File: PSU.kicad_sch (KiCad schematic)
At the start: 97 parts, among them Q1001 2N7002, Q1002 2N7002, Q1003 2N7002, Q1004 2N7002, Q1005 2N7002, Q1006 2N7002, Q1007 AO3407, Q5 2N7002, Q6 2N7002, Q7 NCE30P28Q, SW1001 SW_Push, SW1002 SW_Push, U1001 HM7533HBPR, U1002 SY8253ADC, U1003 SY8253ADC, U1005 TL431DBZ

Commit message: commit before removing duplicated glasgow
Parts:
- renumbered C1039 to C160, C1040 to C161, C1001 to C162, C1002 to C163, C1003 to C164, C1004 to C165, C1005 to C166, C1006 to C167, C1007 to C168, C1008 to C169, C1009 to C170, C1010 to C171, C1011 to C172, C1012 to C173, C1013 to C174, C1014 to C175, C1015 to C176, C1016 to C177, C1017 to C178, C1018 to C179, C1019 to C180, C1020 to C181, C1021 to C182, C1022 to C183, C1023 to C184, D1001 to D27, D1002 to D28, D1003 to D29, D1004 to D30, D23 to D31, D1005 to D32, D1006 to D33, D1007 to D34, D1008 to D35, D1009 to D36, F1001 to F5, JP1001 to JP1, JP1002 to JP2, JP1003 to JP3, L1001 to L3, L1002 to L4, NT1001 to NT2, Q5 to Q1, Q1007 to Q10, Q6 to Q2, Q7 to Q3, Q1001 to Q4, Q1002 to Q5, Q1003 to Q6, Q1004 to Q7, Q1005 to Q8, Q1006 to Q9, R1007 to R100, R1008 to R101, R1009 to R102, R1010 to R103, R1011 to R104, R1012 to R105, R1013 to R106, R1014 to R107, R1015 to R108, R1016 to R109, R1017 to R110, R1018 to R111, R1019 to R112, R1020 to R113, R1021 to R114, R1022 to R115, R1023 to R116, R1024 to R117, R1025 to R118, R1030 to R86, R1031 to R87, R1032 to R88, R1033 to R89, R1034 to R90, R1035 to R91, R1001 to R92, R1002 to R93, R1036 to R94, R1003 to R95, R1004 to R96, R1005 to R97, R54 to R98, R1006 to R99, SW1001 to SW2, SW1002 to SW3, TP1001 to TP22, TP8 to TP23, TP1002 to TP24, TP1003 to TP25, TP1004 to TP26, TP1005 to TP27, U1005 to U39, U1001 to U40, U1002 to U41, U1003 to U42

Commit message: is this a differential pair?
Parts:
- C167: SCH_Show_Footprint (none) -> C0402
- D27: SCH_Show_Footprint (none) -> SMA
- D33: SCH_Show_Footprint (none) -> SOD-323
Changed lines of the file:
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@@
 			)
 		)
+		(property "Field-1" ""
+			(at 255.27 281.94 0)
+			(effects
+				(font
+					(size 1.27 1.27)
+				)
+				(hide yes)
+			)
+		)
+		(property "SCH_Show_Footprint" ""
+			(at 255.27 281.94 0)
+			(effects
+				(font
+					(size 1.27 1.27)
+				)
+				(hide yes)
+			)
+		)
 		(pin "1"
 		)
@@
 			)
 		)
+		(property "Field-1" ""
+			(at 299.72 280.67 0)
+			(effects
+				(font
+					(size 1.27 1.27)
+				)
+				(hide yes)
+			)
+		)
 		(pin "3"
 		)
@@
 			)
 		)
+		(property "Field-1" ""
+			(at 276.86 281.94 0)
+			(effects
+				(font
+					(size 1.27 1.27)
+				)
+				(hide yes)
+			)
+		)
+		(property "SCH_Show_Footprint" ""
+			(at 276.86 281.94 0)
+			(effects
+				(font
+					(size 1.27 1.27)
+				)
+				(hide yes)
+			)
+		)
 		(pin "1"
 		)
@@
 			)
 		)
+		(property "Field-1" ""
+			(at 111.76 127 0)
+			(effects
+				(font
+					(size 1.27 1.27)
+				)
+				(hide yes)
+			)
+		)
+		(property "SCH_Show_Footprint" "SMA"
+			(at 111.76 127 0)
+			(effects
+				(font
+					(size 1.27 1.27)
+				)
+				(hide yes)
+			)
+		)
 		(pin "1"
 		)
@@
 			)
 		)
+		(property "Field-1" ""
+			(at 269.24 281.94 0)
+			(effects
+				(font
+					(size 1.27 1.27)
+				)
+				(hide yes)
+			)
+		)
+		(property "SCH_Show_Footprint" "SOD-323"
+			(at 269.24 281.94 0)
+			(effects
+				(font
+					(size 1.27 1.27)
+				)
+				(hide yes)
+			)
+		)
 		(pin "1"
 		)
@@
 			(at 255.27 294.64 0)
 			(effects
+				(font
+					(size 1.27 1.27)
+				)
+				(hide yes)
+			)
+		)
+		(property "Field-1" ""
+			(at 255.27 294.64 0)
+			(effects
+				(font
+					(size 1.27 1.27)
+				)
+				(hide yes)
+			)
+		)
+		(property "SCH_Show_Footprint" "C0402"
+			(at 255.27 294.64 0)
+			(effects

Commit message: went back to the drawing board
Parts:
- removed C160, C161, C171, C184: 1uF/16V, A_HDJ_Library:C_0402_1005Metric, symbol Device:C
- removed C162, C163, C164, C165: 22uF/25V, Capacitor_SMD:C_0805_2012Metric, symbol Device:C
- removed C166, C168: 2.2uF/50V, A_DFRobot:C_0603, symbol YXD:C
- removed C167: 10uF/10V, A_HDJ_Library:C_0402_1005Metric, symbol Device:C
- removed C169, C170, C179: 100nF/16V, A_HDJ_Library:C_0402_1005Metric, symbol Device:C
- removed C173: 12pF/50V, Capacitor_SMD:C_0402_1005Metric, symbol Device:C
- removed C175, C177, C180, C181, C182, C183: 22uF/10V, A_HDJ_Library:C_0603_1608Metric, symbol Device:C
- removed D27: SMAJ26CA, A_DFRobot:D_SMA, symbol Diode_TVS_AKL:SMAJ24CA
- removed D28, D29, D30: SS54, A_DFRobot:D_SMA, symbol Device:D_Schottky
- removed D31, D34: LED_G, A_HDJ_Library:LED_0603_1608Metric, symbol Device:LED
- removed D33: 1N5819WS, A_DFRobot:D_SOD-323, symbol Diode:1N5819WS
- removed F5: BSMD1206C-2100T, A_DFRobot:R_1206, symbol Device:Fuse
- removed JP1: Jumper_3_Bridged12, A_HDJ_Library:PinHeader_1x03_P2.54mm_Vertical, symbol Jumper:Jumper_3_Bridged12
- removed JP2: Jumper_3_Bridged12, A_DFRobot:PinHeader_1x03_P2.54mm_Vertical, symbol Jumper:Jumper_3_Bridged12
- removed JP3: ~, Connector_PinHeader_2.54mm:PinHeader_2x03_P2.54mm_Vertical, symbol YXD:Pin_2*3
- removed L3, L4: 2.2uH/4.3A, A_HDJ_Library:L_Sunlord_SWPA4020S, symbol Device:L
- removed NT2: NetTie_2, NetTie:NetTie-3_SMD_Pad2.0mm, symbol Device:NetTie_2
- removed Q1, Q2, Q5, Q6, Q7, Q8, Q9: 2N7002, Package_TO_SOT_SMD:SOT-23, symbol Transistor_FET:2N7002
- removed Q10: AO3407, Package_TO_SOT_SMD:SOT-23, symbol Transistor_FET:Q_PMOS_GSD
- removed Q3: NCE30P28Q, A_HDJ_Library:MOSFET_PDFN8_3.3x3.3, symbol Transistor_FET:AON7262E
- removed R101: 1M/1%, A_DFRobot:R_0402, symbol Device:R
- removed R102, R91, R94, R99: 100K/1%, A_DFRobot:R_0402, symbol Device:R
- removed R103, R104, R95: 1K/1%, A_DFRobot:R_0402, symbol Device:R
- removed R105, R110, R118, R86, R88, R97: 10K/1%, A_DFRobot:R_0402, symbol Device:R
- removed R106: 470R/1%, A_DFRobot:R_0402, symbol Device:R
- removed R107, R87: 2.2K/1%, A_DFRobot:R_0402, symbol Device:R
- removed R108, R113, R92, R93, R96: 100R/1%, A_DFRobot:R_0402, symbol Device:R
- removed R111, R89, R90, R98: 21.5K/1%, A_DFRobot:R_0402, symbol Device:R
- removed R112: 4.7K/1%, A_DFRobot:R_0402, symbol Device:R
- removed R115: 200R/1%, A_DFRobot:R_0402, symbol YXD:R
- removed TP22, TP23, TP24, TP25, TP26, TP27: TestPoint, A_HDJ_Library:TestPoint_Pad_D1.5mm, symbol Connector:TestPoint
- removed U39: TL431DBZ, A_HDJ_Library:SOT-23, symbol Reference_Voltage:TL431DBZ
- removed U40: HM7533HBPR, Package_TO_SOT_SMD:SOT-89-3, symbol YXD:HM7533
- removed U41, U42: SY8253ADC, A_HDJ_Library:TSOT-23-6, symbol Regulator_Switching:LM2734X
- added C1: 0.1uF, A_HDJ_Library:C_0402_1005Metric, symbol Device:C
- added C2: 10uF, Capacitor_SMD:C_0805_2012Metric, symbol Device:C
- added C3, C4, C5, C6: 10uF 25V, Capacitor_SMD:C_0805_2012Metric, symbol Device:C
- added C401: 100nF/50V, A_HDJ_Library:C_0402_1005Metric, symbol Device:C
- added C408: 22uF/50V, Capacitor_SMD:C_0805_2012Metric, symbol Device:C
- added C410, C411, C412, C413: 1uF/50V, A_HDJ_Library:C_0402_1005Metric, symbol Device:C
- added C414, C415: 0.1uf, A_HDJ_Library:C_0402_1005Metric, symbol Device:C
- added C416, C417: 100uF, A_HDJ_Library:C_0402_1005Metric, symbol Device:C
- added L401: 6.8uH/4.5A, Inductor_SMD:L_6.3x6.3_H3, symbol Device:L
- added R402: 19.1K/1%, A_HDJ_Library:R_0402_1005Metric, symbol Device:R
- added R405, R408: 1K/1%, A_HDJ_Library:R_0402_1005Metric, symbol Device:R
- added R409: 10K/1%, A_HDJ_Library:R_0402_1005Metric, symbol Device:R
- added U3: TPPM0110DWPR, DWP20_3P81X2P79, symbol 2026-04-06_00-39-49:TPPM0110DWPR
- added U402: AP7381-33SA-7, Package_TO_SOT_SMD:SOT-23, symbol Regulator_Linear:AP7381-33SA-7
- added U403: AP63200WU, Package_TO_SOT_SMD:TSOT-23-6, symbol Regulator_Switching:AP63200WU
- C402: renamed from C172; value 12pF/50V -> 47pF/50V; footprint Capacitor_SMD:C_0402_1005Metric -> A_HDJ_Library:C_0402_1005Metric; DF_Comment 贴片电容0402-12pF-50V-NPO(0402) -> (none); Digikey (none) -> 490-5942-1-ND; now fitted; now in the parts list
- C403: renamed from C174; DF_Comment 贴片电容0603-22uF-10V-X5R(0603) -> (none); Digikey (none) -> 490-10476-1-ND
- C404: renamed from C176; DF_Comment 贴片电容0603-22uF-10V-X5R(0603) -> (none); Digikey (none) -> 490-10476-1-ND
- C405: renamed from C178; value 100nF/16V -> 100nF/50V; DF_Comment 贴片电容0402-100nF-16V-X7R(0402) -> (none); Digikey (none) -> 478-KGM05CR71H104KHCT-ND
- D401: renamed from D35; value 0402ESDA-05N -> ESD5V0B03; DF_Comment 5.0V双向静电保护管_0402ESDA-05N -> (none); Digikey (none) -> ESD9B5.0ST5GOSCT-ND
- D402: renamed from D36; value 0402ESDA-05N -> ESD5V0B03; DF_Comment 5.0V双向静电保护管_0402ESDA-05N -> (none); Digikey (none) -> ESD9B5.0ST5GOSCT-ND
- D403: renamed from D32; value LED_R -> LED_G; DF_Comment 贴片LED红色0603(0603) -> (none); Digikey (none) -> 160-1479-1-ND
- Q401: renamed from Q4; footprint Package_TO_SOT_SMD:SOT-23 -> A_HDJ_Library:SOT-23; DF_Comment 2N7002-N沟道MOS管-SOT-23[备选型号:JMTL2N7002K] -> (none); Digikey (none) -> 2N7002-TPMSCT-ND
- R401: renamed from R109; value 75K/1% -> 100K/1%; footprint A_DFRobot:R_0402 -> A_HDJ_Library:R_0402_1005Metric; DF_Comment 贴片电阻0402-75K-1% -> (none); Digikey (none) -> 311-100KJRCT-ND
- R403: renamed from R114; DF_Comment 贴片电阻0402-10K-1% -> (none)
- R404: renamed from R117; DF_Comment 贴片电阻0402-10K-1% -> (none)
- R406: renamed from R116; value 100R/1% -> 1K/1%; footprint A_DFRobot:R_0402 -> A_HDJ_Library:R_0402_1005Metric; DF_Comment 贴片电阻0402-100R-1% -> (none); Digikey (none) -> 311-1.0KJRCT-ND
- R407: renamed from R100; value 2.2K/1% -> 1K/1%; footprint A_DFRobot:R_0402 -> A_HDJ_Library:R_0402_1005Metric; DF_Comment 贴片电阻0402-2.2K-1% -> (none); Digikey (none) -> 311-1.0KJRCT-ND
- SW401: renamed from SW2; footprint A_DFRobot:SW_PUSH_SIDE_TS-1012EV_7.7x3.95x3.5mm -> Button_Switch_THT:SW_PUSH_6mm; DF_Comment 侧按卧插4脚开关-TS-1012EV-26-7*3.5*3.5 -> (none); Digikey (none) -> 450-1644-ND
- SW402: renamed from SW3; footprint A_DFRobot:SW_PUSH_SIDE_TS-1012EV_7.7x3.95x3.5mm -> Button_Switch_THT:SW_PUSH_6mm; DF_Comment 侧按卧插4脚开关-TS-1012EV-26-7*3.5*3.5 -> (none); Digikey (none) -> 450-1644-ND
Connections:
- net +3V3_ROM is gone; now on net +3V3: R407.2
- net QGND is gone; now on net GND: C403.1, C404.1, C405.2, D401.1 (A1), D402.1 (A1), Q401.2 (S), SW401.2, SW402.2
- net +12V: now also C1.1, C2.2, C3.2, C4.2, C408.2, C412.1, C5.2, C6.2, U402.1 (VI), U403.2 (EN), U403.3 (IN)
- net +3V3: now also C413.1, C415.2, C417.1, U3.4 (3.3VOUT), U402.2 (VO)
- net +5V: now also L401.2, U3.6 (5VCC)
- net GND: now also C1.2, C2.1, C3.1, C4.1, C408.1, C410.2, C411.2, C412.2, C413.2, C414.1, C415.1, C416.2, C417.2, C5.1, C6.1, R402.1, R409.1, U3.20 (GND), U402.3 (GND), U403.4 (GND)
- net ~{PWR_LED}/~{PSON}: now also R408.1
- net ~{PWR_SW}: now also R405.2
- net at C402.2, R401.1: now also R402.2, U403.1 (FB)
- net at Q401.1 (G): now also R408.2, R409.2
- net POWER_SW: no longer names the net of D401.2 (A2), R403.1, SW401.1
- net POWER_SW: now also C410.1, R405.1
- net RESET_SW: no longer names the net of D402.2 (A2), R404.1, R406.1, SW402.1
- net RESET_SW: now also C411.1
- new net: C401.1, L401.1, U403.5 (SW)
- new net: C401.2, U403.6 (BST)
- new net +1V8: C414.2, C416.1, U3.8 (1.8VOUT)
- no-connect marks 1 -> 0
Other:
- note added: "AP63300 32V 3A 500kHz"
- note added: "LattePanda Mu has integrated pull-up resistors."
- note added: "alternatives? Diodes AP63300 (different vFB)"
- note removed: "12V DC Input(12V 6A-10A)"
- note removed: "Auto PowerUp"
- note removed: "LattePanda Mu has integrated pull-up resistors. Do not solder resistors R50 and R56!"
- note removed: "Power for PCIe x4 OVP@13.86V"
- note removed: "Pullup power for bios_sel"
- note removed: "SY8253ADC 23V 3A 500kHz"
- note removed: "Vout=0.6*(21.5+4.7)/4.7=3.446V"
- note removed: "Vout=0.6*(75+10)/10=5.1V"
- note removed: "soft start"
- moved on the sheet: C403, C404, C405, D401, D402, D403, Q401, R401, R403, R404, R406, R407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

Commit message: some power stuff (unfinished)
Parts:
- added C10, C12, C8, C9: 22uF, 25V, Capacitor_SMD:C_1206_3216Metric, symbol Device:C
- added C40, C41, C42: 1uF, A_DFRobot:C_0402_1005Metric, symbol Device:C
- added C43: 10v 0.1uF, A_DFRobot:C_0402_1005Metric, symbol Device:C
- added C44, C45, C46, C47, C48, C51, C52, C53: 10V 47uF, Capacitor_SMD:C_1210_3225Metric, symbol Device:C
- added C7: 330uF 25V, Capacitor_SMD:CP_Elec_8x11.9, symbol Device:C
- added L1: 550nH, Inductor_SMD:L_Coilcraft_XAL7070-XXX, symbol Device:L
- added NT1: NetTie_2, symbol Device:NetTie_2
- added R16: 200k, A_DFRobot:R_0402_1005Metric, symbol Device:R
- added R18: 100k, A_DFRobot:R_0402_1005Metric, symbol Device:R
- added R19, R20: 0, A_DFRobot:R_0402_1005Metric, symbol Device:R
- added U4: TPS548A23VANR, VAN0019A-MFG, symbol 2026-04-07_02-11-45:TPS548A23VANR
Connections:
- net +12V: now also C10.1, C12.1, C40.1, C41.1, C7.1, C8.1, C9.1, R16.1, U4.12 (VIN), U4.4 (VIN)
- net GND: now also C10.2, C12.2, C40.2, C41.2, C42.1, C44.1, C45.1, C46.1, C47.1, C48.1, C51.1, C52.1, C53.1, C7.2, C8.2, C9.2, R18.2, U4.14 (CFG4)
- new net: C43.1, R19.2
- new net: C43.2, L1.1, U4.7 (SW), U4.8 (SW), U4.9 (SW)
- new net: R19.1, U4.10 (BST)
- new net: R16.2, R18.1, U4.16 (EN)
- new net: C42.2, U4.13 (CFG3), U4.15 (CFG5), U4.6 (VCC)
- new net +5V_highpower: C44.2, C45.2, C46.2, C47.2, C48.2, C51.2, C52.2, C53.2, L1.2

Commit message: power finished started diff pairs
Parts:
- added NT2: NetTie_2, symbol Device:NetTie_2
- added NT3: NetTie_2, NetTie:NetTie-2_SMD_Pad0.5mm, symbol Device:NetTie_2
- added R21: 10, A_DFRobot:R_0402_1005Metric, symbol Device:R
- added R22: 10k, A_DFRobot:R_0402_1005Metric, symbol Device:R
- added R23: 0, A_DFRobot:R_0402_1005Metric, symbol Device:R
- NT1: footprint (none) -> NetTie:NetTie-2_SMD_Pad0.5mm
- U4: footprint VAN0019A-MFG -> PowerShit:VAN0019A-MFG
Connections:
- net +5V_highpower: now also NT1.2
- net GND: now also U4.11 (PGND), U4.5 (PGND), NT2.1, NT3.2; no longer U4.14 (CFG4)
- net at R20.1: now also U4.17 (VOS_FB)
- net at R20.2: now also R21.1
- net 5vcc: now reaches C42.2, U4.13 (CFG3), U4.15 (CFG5), U4.6 (VCC)
- net 5vcc: now also R22.2
- net at NT1.1: now also R21.2
- net at U4.1 (PG): now also R22.1
- net at U4.18 (GOS): now also R23.1
- net 5agnd: now reaches U4.19 (AGND)
- net 5agnd: now also U4.14 (CFG4), NT2.2
- new net: NT3.1, R23.2

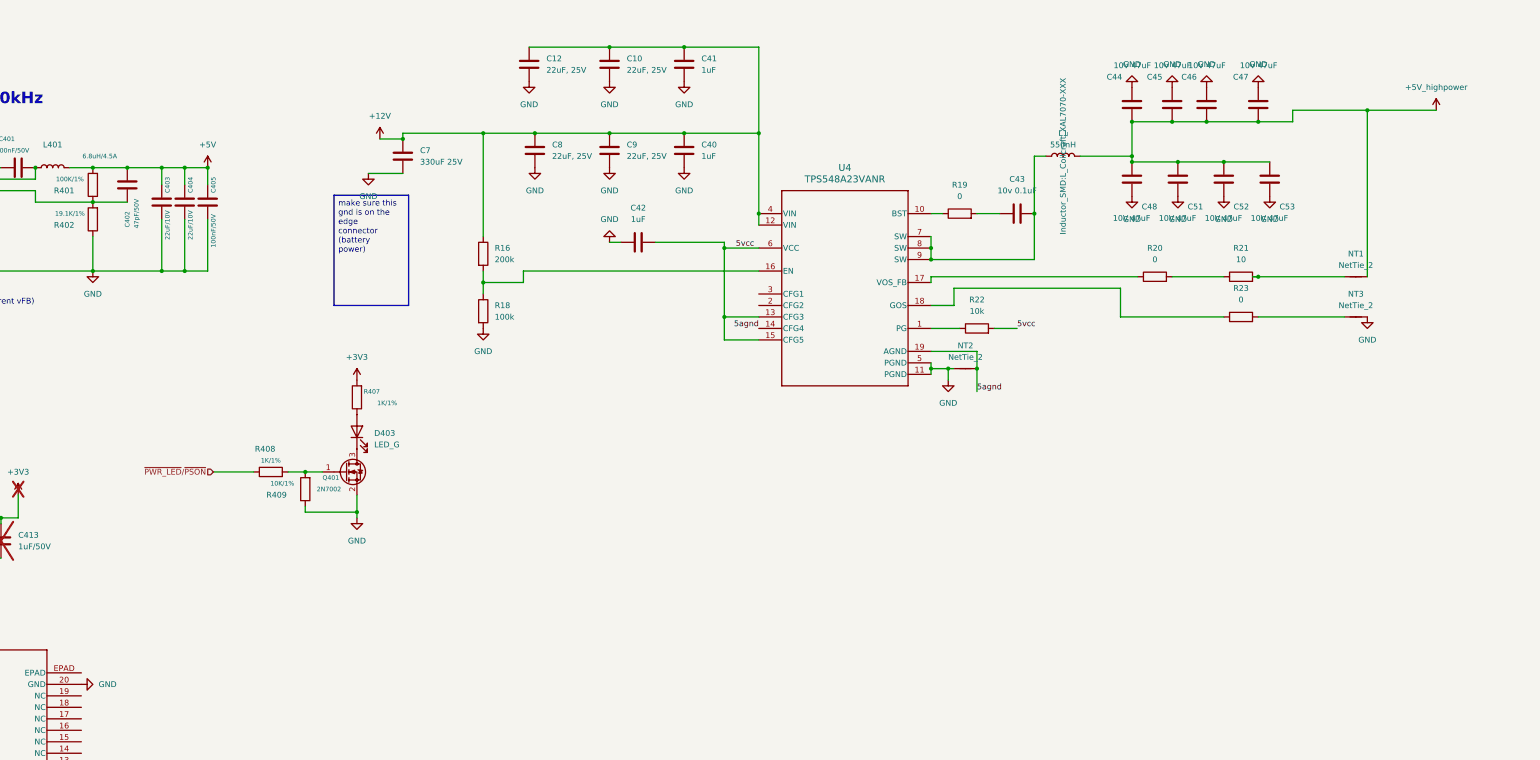
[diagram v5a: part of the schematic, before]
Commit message: fixed 5v->3v bug
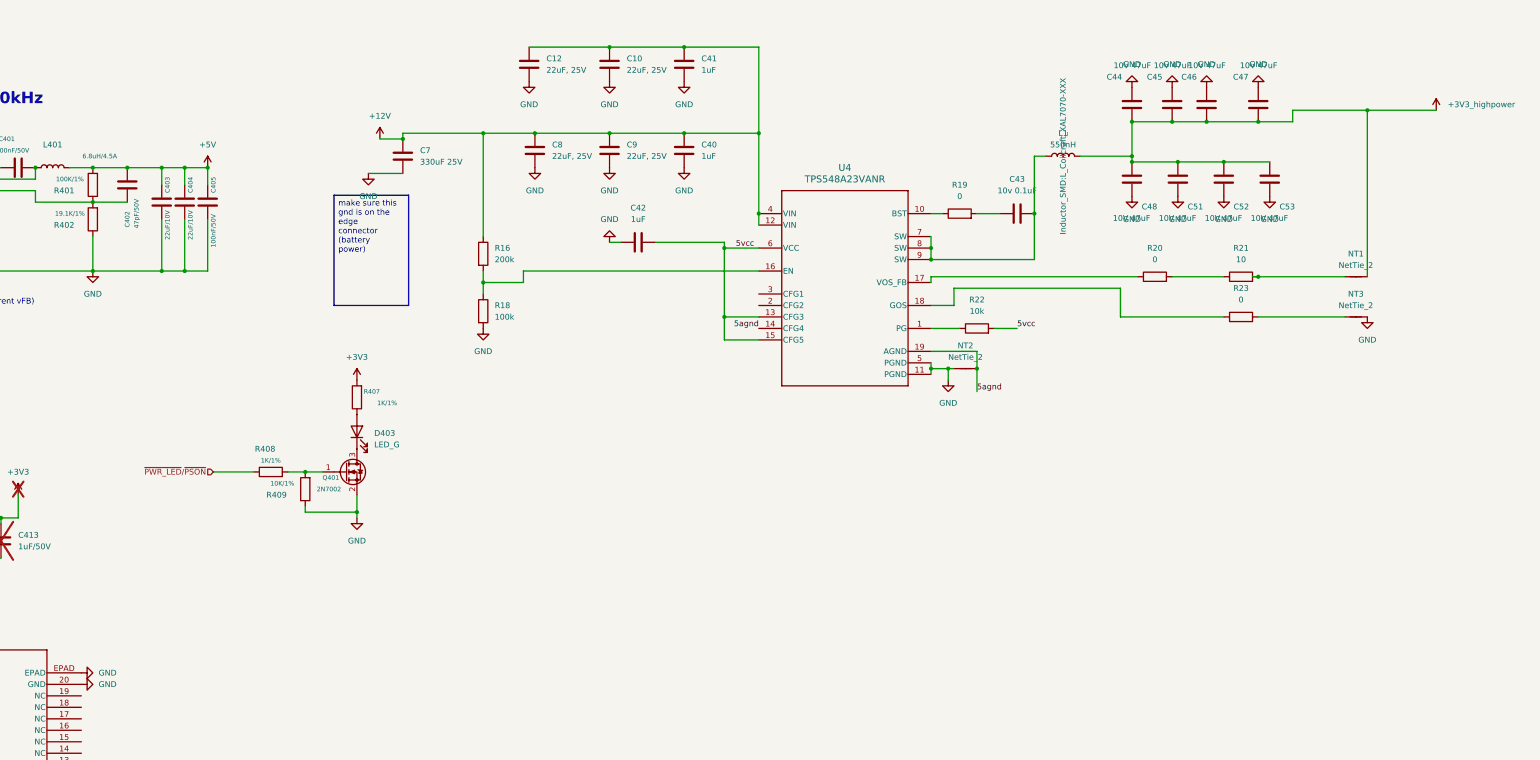
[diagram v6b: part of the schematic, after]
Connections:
- net GND: now also U3.EPAD
- net +5V_highpower renamed +3V3_highpower
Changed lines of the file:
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@@
 	(symbol
 		(lib_id "power:GND")
+		(at 262.89 298.45 90)
+		(unit 1)
+		(body_style 1)
+		(exclude_from_sim no)
+		(in_bom yes)
+		(on_board yes)
+		(in_pos_files yes)
+		(dnp no)
+		(fields_autoplaced yes)
+		(property "Reference" "#PWR0323"
+			(at 269.24 298.45 0)
+			(hide yes)
+			(show_name no)
+			(do_not_autoplace no)
+			(effects
+				(font
+					(size 1.27 1.27)
+				)
+			)
+		)
+		(property "Value" "GND"
+			(at 266.7 298.4499 90)
+			(show_name no)
+			(do_not_autoplace no)
+			(effects
+				(font
+					(size 1.27 1.27)
+				)
+				(justify right)
+			)
+		)
+		(property "Footprint" ""
+			(at 262.89 298.45 0)
+			(hide yes)
+			(show_name no)
+			(do_not_autoplace no)
+			(effects
+				(font
+					(size 1.27 1.27)
+				)
+			)
+		)
+		(property "Datasheet" ""
+			(at 262.89 298.45 0)
+			(hide yes)
+			(show_name no)
+			(do_not_autoplace no)
+			(effects
+				(font
+					(size 1.27 1.27)
+				)
+			)
+		)
+		(property "Description" "Power symbol creates a global label with name \"GND\" , ground"
+			(at 262.89 298.45 0)
+			(hide yes)
+			(show_name no)
+			(do_not_autoplace no)
+			(effects
+				(font
+					(size 1.27 1.27)
+				)
+			)
+		)
+		(pin "1"
+		)
+		(instances
+			(project "microcyber"
+				(path "/7ac319af-771c-4997-a005-b73a4a9b44ab/bf9d2aec-36d6-402d-b3de-6cf70c51ac31"
+					(reference "#PWR0323")
+					(unit 1)
+				)
+			)
+		)
+	)
+	(symbol
+		(lib_id "power:GND")
 		(at 361.95 167.64 0)
 		(unit 1)
@@
 			)
 		)
-		(property "Value" "+5V_highpower"
-			(at 562.61 168.91 0)
+		(property "Value" "+3V3_highpower"
+			(at 565.15 172.7199 0)
 			(show_name no)
 			(do_not_autoplace no)
@@
 					(size 1.27 1.27)
 				)
+				(justify left)
 			)
 		)

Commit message: hdmi diff pair remains??
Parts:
- added J6: Conn_01x01_Socket, Connector_PinHeader_2.00mm:PinHeader_1x01_P2.00mm_Horizontal, symbol Connector:Conn_01x01_Socket
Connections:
- net +5V: now also J6.1 (Pin_1)
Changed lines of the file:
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@@
+	)
+	(symbol
+		(lib_id "Connector:Conn_01x01_Socket")
+		(at 295.91 186.69 0)
+		(unit 1)
+		(body_style 1)
+		(exclude_from_sim no)
+		(in_bom yes)
+		(on_board yes)
+		(in_pos_files yes)
+		(dnp no)
+		(fields_autoplaced yes)
+		(property "Reference" "J6"
+			(at 297.18 185.4199 0)
+			(show_name no)
+			(do_not_autoplace no)
+			(effects
+				(font
+					(size 1.27 1.27)
+				)
+				(justify left)
+			)
+		)
+		(property "Value" "Conn_01x01_Socket"
+			(at 297.18 187.9599 0)
+			(show_name no)
+			(do_not_autoplace no)
+			(effects
+				(font
+					(size 1.27 1.27)
+				)
+				(justify left)
+			)
+		)
+		(property "Footprint" "Connector_PinHeader_2.00mm:PinHeader_1x01_P2.00mm_Horizontal"
+			(at 295.91 186.69 0)
+			(hide yes)
+			(show_name no)
+			(do_not_autoplace no)
+			(effects
+				(font
+					(size 1.27 1.27)
+				)
+			)
+		)
+		(property "Datasheet" ""
+			(at 295.91 186.69 0)
+			(hide yes)
+			(show_name no)
+			(do_not_autoplace no)
+			(effects
+				(font
+					(size 1.27 1.27)
+				)
+			)
+		)
+		(property "Description" "Generic connector, single row, 01x01, script generated"
+			(at 295.91 186.69 0)
+			(hide yes)
+			(show_name no)
+			(do_not_autoplace no)
+			(effects
+				(font
+					(size 1.27 1.27)
+				)
+			)
+		)
+		(pin "1"
+		)
+		(instances
+			(project "microcyber"
+				(path "/7ac319af-771c-4997-a005-b73a4a9b44ab/bf9d2aec-36d6-402d-b3de-6cf70c51ac31"
+					(reference "J6")
+					(unit 1)
+				)
+			)
+		)
 	)
 	(symbol

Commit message: last push before editing with the grid view (gonna break everything)
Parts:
- C1: value 0.1uF -> u1; MPN (none) -> C1005X7R1H104K050BE
- C10, C12, C8, C9: value 22uF, 25V -> 22u; MPN (none) -> GRM31CC81E226ME11L
- C2: value 10uF -> 10u; MPN (none) -> C2012X5R1E106K125AB
- C3, C4, C5, C6: value 10uF 25V -> 10u; MPN (none) -> C2012X5R1E106K125AB
- C40, C41, C42: value 1uF -> 1u; MPN (none) -> GRM155C81E105KE11D
- C401, C405: value 100nF/50V -> 100n; MPN (none) -> 478-KGM05CR71H104KHCT-ND
- C402: value 47pF/50V -> 47p; MPN (none) -> 490-5942-1-ND
- C403, C404: value 22uF/10V -> 22u; MPN (none) -> 490-10476-1-ND
- C408: value 22uF/50V -> 22u; MPN (none) -> 445-14428-1-ND
- C410: value 1uF/50V -> 1u; Digikey 490-GRM155R61H105KE05DCT-ND -> (none); MPN (none) -> 490-GRM155R61H105KE05DCT-ND
- C411: value 1uF/50V -> 1u; MPN (none) -> 490-GRM155R61H105KE05DCT-ND
- C414, C415: value 0.1uf -> u1; MPN (none) -> 490-GRM155R61H105KE05DCT-ND
- C416, C417: value 100uF -> 100u; MPN (none) -> 490-GRM155R61H105KE05DCT-ND
- C43: value 10v 0.1uF -> u1; MPN (none) -> C1005X5R1A104K050BA
- C44, C45, C46, C47, C48, C51, C52, C53: value 10V 47uF -> 47u; MPN (none) -> GRM32ER71A476ME15L
- C7: value 330uF 25V -> 330u; MPN (none) -> A768KS337M1ELAE019
- D401, D402: MPN (none) -> ESD5V0B03
- D403: Digikey 160-1479-1-ND -> (none); MPN (none) -> 150060BS75000
- L1: MPN (none) -> XAL7070-551MEB
- L401: value 6.8uH/4.5A -> 6uH8; MPN (none) -> 553-BMRA000606306R8MA1CT-ND
- Q401: MPN (none) -> 2N7002
- R16: value 200k -> 200K; MPN (none) -> CRCW0402200KFKED
- R18: value 100k -> 100K; MPN (none) -> ERJ-2RKF1003X
- R19, R20, R23: MPN (none) -> MCS0402HZ0000ZE100
- R21: MPN (none) -> CRCW040210R0FKED
- R22: value 10k -> 10K; MPN (none) -> ERJPA2F1002X
- R401: value 100K/1% -> 100K; MPN (none) -> 311-100KJRCT-ND
- R402: value 19.1K/1% -> 19K1; MPN (none) -> 13-RC0402FR-1319K1LCT-ND
- R405: value 1K/1% -> 1K; Digikey 311-1.0KJRCT-ND -> (none); MPN (none) -> 311-1.0KJRCT-ND
- R406, R407, R408: value 1K/1% -> 1K; MPN (none) -> 311-1.0KJRCT-ND
- R409: value 10K/1% -> 10K; MPN (none) -> 311-10KJRCT-ND
- SW401, SW402: MPN (none) -> 450-1644-ND
- U403: MPN (none) -> AP63200WU
